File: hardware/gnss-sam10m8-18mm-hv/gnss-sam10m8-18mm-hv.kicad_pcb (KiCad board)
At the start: 4 copper layers, 22 x 27.5 mm, 34 parts, among them J3 BM05B-SRSS-TB, U1 SAM-M10Q-00B, U3 TPS62913RPUR

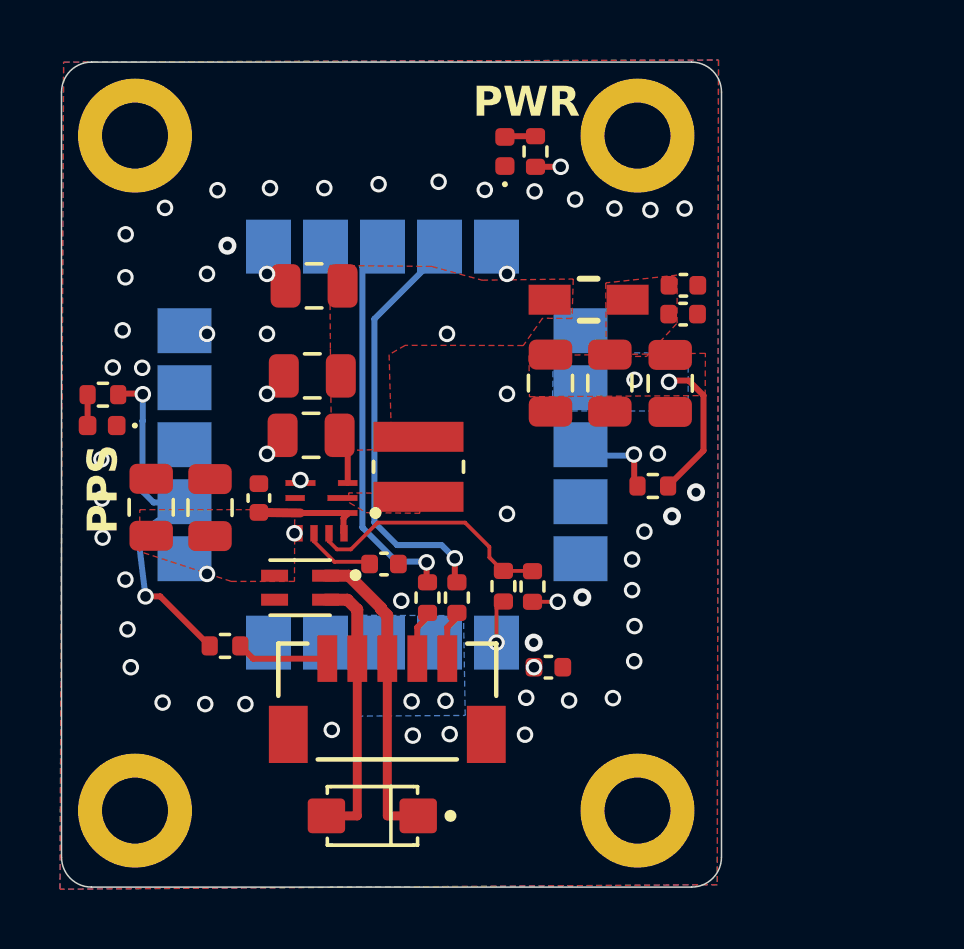
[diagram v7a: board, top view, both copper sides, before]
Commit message: hardware(gnss-sam10m8): silkscreen -- the board can now be identified assembled
Review finding B6. The only board-identifying text was on B.SilkS at
(53.15, 43.29), dead centre under U1, which spans 45.1-60.6 x 34.5-50.0 -- it
was completely covered by the module. All 34 reference designators were hidden.

This stopped being cosmetic once J3 pin 5 became TIMEPULSE. gnss-px1105r is the
same 22.00 x 27.50 mm outline with the same BM05B-SRSS-TB on the same pins, but
drives that pin as RXD2 for RTK corrections. Plugging the wrong board into the
harness means the host drives TIMEPULSE, and since TIMEPULSE shares the die with
SAFEBOOT_N, a low at startup puts the receiver into safeboot -- a silent
functional failure, not a visible one.

- Board ID moved to a B.SilkS strip below the module (52.5, 51.4..54.1), which
  is the only area large enough that U1 does not cover: "TinkerRocket /
  SAM-M10Q ${REVISION} / ANTENNA SIDE".
- "SAM-M10Q" added to F.SilkS at the top so the board is identifiable without
  flipping it.
- ANTENNA SIDE records that the patch looks out of the B.Cu face. Nothing on the
  board said which way was up.
- Reference designators made visible for U1, U3, J3, L8, FB1, CR1, R9 and C16,
  repositioned into free silk and set to 0.85 mm (the board minimum is 0.8).
- J3 pin-1 marker added at (56.30, 48.10).

DRC improves on the pre-existing baseline: 6 warnings against 9. The 5 silk
warnings are gone; what remains is 5 lib_footprint_mismatch and 1 silk_over_copper
(U3's outline circle over L8's pad, pre-existing). 0 unconnected items,
0 schematic-parity issues.

Co-Authored-By: Claude Opus 5 <noreply@anthropic.com>
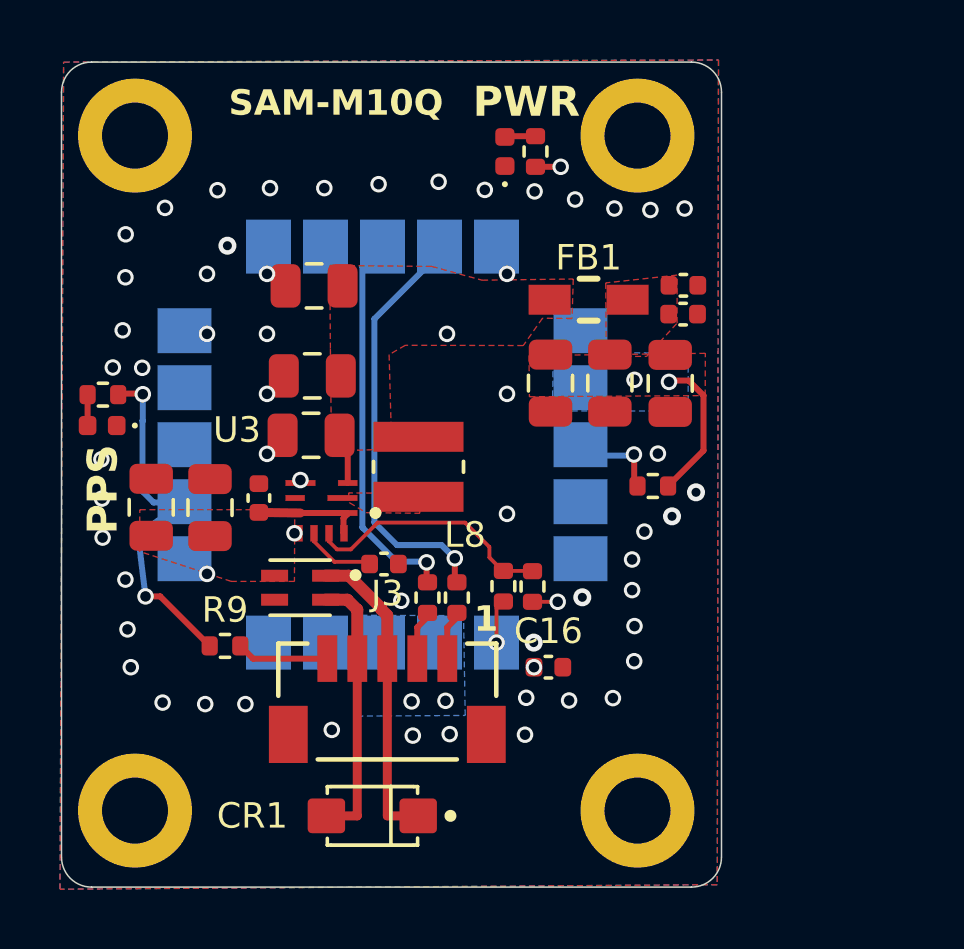
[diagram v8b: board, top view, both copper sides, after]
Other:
- board text added: "1"
- board text added: "ANTENNA SIDE"
- board text added: "SAM-M10Q"
- board text added: "SAM-M10Q ${REVISION}"
- board text added: "TinkerRocket"
- board text removed: "TinkerRocket GNSS SAM-M10Q ${REVISION}"
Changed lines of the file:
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@@
 		(at 54.05 43.03 90)
 		(property "Reference" "L8"
-			(at 0.282 -2.4064 90)
+			(at -2.27 1.55)
 			(layer "F.SilkS")
-			(hide yes)
 			(effects
 				(font
-					(size 0.64 0.64)
+					(size 0.85 0.85)
 					(thickness 0.15)
 				)
@@
 		(at 50.815 44.32 180)
 		(property "Reference" "U3"
-			(at 0.074 -1.9548 0)
+			(at 2.815 2.52)
 			(layer "F.SilkS")
-			(hide yes)
 			(effects
 				(font
-					(size 0.48 0.48)
-					(thickness 0.12)
+					(size 0.85 0.85)
+					(thickness 0.15)
 				)
 			)
@@
 		(at 52.51 54.665 180)
 		(property "Reference" "CR1"
-			(at 0.635 -2.032 0)
+			(at 4.0 0.0)
 			(layer "F.SilkS")
-			(hide yes)
 			(effects
 				(font
-					(size 1 1)
+					(size 0.85 0.85)
 					(thickness 0.15)
 				)
@@
 		(at 59.72 37.46)
 		(property "Reference" "FB1"
-			(at 0 -1.835 0)
+			(at 0.0 -1.4)
 			(layer "F.SilkS")
-			(hide yes)
 			(effects
 				(font
-					(size 1 1)
+					(size 0.85 0.85)
 					(thickness 0.15)
 				)
@@
 		(tags "BM05B-SRSS-TB ")
 		(property "Reference" "J3"
-			(at 0 -1.4284 0)
+			(at 0.0 -3.6)
 			(unlocked yes)
 			(layer "F.SilkS")
-			(hide yes)
 			(effects
 				(font
-					(size 1 1)
+					(size 0.85 0.85)
 					(thickness 0.15)
 				)
@@
 		(tags "resistor")
 		(property "Reference" "R9"
-			(at 0 -1.17 0)
+			(at 0.0 -1.2)
 			(layer "F.SilkS")
-			(hide yes)
 			(effects
 				(font
-					(size 1 1)
+					(size 0.85 0.85)
 					(thickness 0.15)
 				)
@@
 		(tags "capacitor")
 		(property "Reference" "C16"
-			(at 0 -1.16 0)
+			(at 0.0 -1.2)
 			(layer "F.SilkS")
-			(hide yes)
 			(effects
 				(font
-					(size 1 1)
+					(size 0.85 0.85)
 					(thickness 0.15)
 				)
@@
 			(at -4.825 8.885 90)
 			(layer "B.SilkS")
-			(hide yes)
 			(effects
 				(font
-					(size 1 1)
+					(size 0.85 0.85)
 					(thickness 0.15)
 				)
@@
 		)
 	)
-	(gr_text "TinkerRocket\nGNSS SAM-M10Q\n${REVISION}"
-		(at 53.15 43.29 0)
-		(layer "B.SilkS")
-		(effects
-			(font
-				(size 1 1)
-				(thickness 0.2)
-				(bold yes)
-			)
-			(justify mirror)
-		)
-	)
 	(segment
 		(start 62.445 40.155)
@@
 		(net "Net-(J3-Pad5)")
 	)
+	(gr_text "TinkerRocket"
+		(at 52.5 51.4 0)
+		(layer "B.SilkS")
+		(effects
+			(font
+				(size 0.85 0.85)
+				(thickness 0.15)
+				(bold yes)
+			)
+			(justify mirror)
+		)
+	)
+	(gr_text "SAM-M10Q ${REVISION}"
+		(at 52.5 52.75 0)
+		(layer "B.SilkS")
+		(effects
+			(font
+				(size 0.85 0.85)
+				(thickness 0.15)
+			)
+			(justify mirror)
+		)
+	)
+	(gr_text "ANTENNA SIDE"
+		(at 52.5 54.1 0)
+		(layer "B.SilkS")
+		(effects
+			(font
+				(size 0.85 0.85)
+				(thickness 0.15)
+			)
+			(justify mirror)
+		)
+	)
+	(gr_text "SAM-M10Q"
+		(at 51.3 30.9 0)
+		(layer "F.SilkS")
+		(effects
+			(font
+				(size 0.85 0.85)
+				(thickness 0.15)
+				(bold yes)
+			)
+		)
+	)
+	(gr_text "1"
+		(at 56.3 48.1 0)
+		(layer "F.SilkS")
+		(effects
+			(font
+				(size 0.85 0.85)
+				(thickness 0.15)
+				(bold yes)
+			)
+		)
+	)
 	(zone
